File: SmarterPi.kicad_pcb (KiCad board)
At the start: 2 copper layers, 56 x 65 mm, 8 parts, among them J1 Raspberry_Pi_2_3, J2 RJ10

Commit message: Reed
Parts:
- added J3: Screw_Terminal_01x02, TerminalBlock:TerminalBlock_bornier-2_P5.08mm, F.Cu at (92.3, 80.2)
- added J4: Screw_Terminal_01x02, TerminalBlock:TerminalBlock_bornier-2_P5.08mm, F.Cu at (105.8, 80.2)
- added R1: 2k4, Resistor_THT:R_Axial_DIN0207_L6.3mm_D2.5mm_P10.16mm_Horizontal, F.Cu at (89.8, 86.1)
- added REF**: KiCad-Logo2_8mm_SilkScreen, Symbol:KiCad-Logo2_8mm_SilkScreen, B.Cu at (110.5, 130.1)
- moved REF** 2.99 mm to (128.0, 131.1)
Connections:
- J1 pad 15: Net-(J1-Pad15) -> REED
- J1 pad 17: +3V3 -> Net-(J1-Pad17)
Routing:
- net REED: track 0.00 -> 45.2 mm
- net +3V3: track 18.7 -> 63.0 mm
- net +5V: track 0.00 -> 2.54 mm
- added copper zone on B.Cu, net GND
- added copper zone on F.Cu, net GND
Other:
- board text added: "B"
- board text added: "G"
- board text added: "GPIO22 = Reed (pulled down)"
- board text added: "haus-automatisierung.com - v0.1"
- board text removed: "v0.1"

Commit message: 1Wire
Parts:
- added R2: 4,7kΩ, Resistor_THT:R_Axial_DIN0207_L6.3mm_D2.5mm_P10.16mm_Horizontal, F.Cu at (89.5, 86.1)
- J3: value Screw_Terminal_01x02 -> Screw_Terminal_01x04; footprint TerminalBlock:TerminalBlock_bornier-2_P5.08mm -> TerminalBlock_Phoenix:TerminalBlock_Phoenix_MPT-0,5-4-2.54_1x04_P2.54mm_Horizontal
- J4: value Screw_Terminal_01x02 -> Screw_Terminal_01x03; footprint TerminalBlock:TerminalBlock_bornier-2_P5.08mm -> TerminalBlock_Phoenix:TerminalBlock_Phoenix_MPT-0,5-3-2.54_1x03_P2.54mm_Horizontal
- R1: value 2k4 -> 2,4kΩ
- moved R1 23.3 mm to (113.1, 86.1), turned to 180 degrees
- moved J3 19.5 mm to (111.8, 80.5), turned to 180 degrees
- moved J4 8.70 mm to (97.2, 80.5), turned to 180 degrees
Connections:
- J1 pad 7: Net-(J1-Pad7) -> 1Wire
- J4 pad 1: Net-(J4-Pad1) -> +3V3
- J4 pad 2: Net-(J4-Pad2) -> 1Wire
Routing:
- net 1Wire: track 0.00 -> 56.3 mm
- net REED: track 45.2 -> 42.0 mm
- net Net-(J3-Pad4): track 0.00 -> 0.94 mm
- net +3V3: track 63.0 -> 62.5 mm
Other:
- board text added: "+"
- board text added: "1Wire"
- board text added: "D"
- board text added: "GND"
- board text added: "GPIO22 = Reed (pulled down) GPIO4 = 1Wire"
- board text added: "REED"
- board text removed: "GPIO22 = Reed (pulled down)"

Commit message: Readme, License, Preview
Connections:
- J4 pad 1: +3V3 -> +5V
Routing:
- net +5V: track 2.54 -> 42.7 mm
- net +3V3: track 62.5 -> 52.8 mm
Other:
- board text added: "2.4kΩ"
- board text added: "4.7kΩ"
- board text added: "VCC"
- board text removed: "+"

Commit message: Added LEDs
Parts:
- added D1: LED, LED_SMD:LED_0805_2012Metric_Pad1.15x1.40mm_HandSolder, F.Cu at (123.6, 116.7)
- added D2: LED, LED_SMD:LED_0805_2012Metric_Pad1.15x1.40mm_HandSolder, F.Cu at (123.7, 119.2)
- added D3: LED, LED_SMD:LED_0805_2012Metric_Pad1.15x1.40mm_HandSolder, F.Cu at (123.7, 121.7)
- added R3: 330Ω, Resistor_SMD:R_0805_2012Metric_Pad1.20x1.40mm_HandSolder, F.Cu at (128.1, 116.7)
- added R4: 330Ω, Resistor_SMD:R_0805_2012Metric_Pad1.20x1.40mm_HandSolder, F.Cu at (128.1, 119.2)
- added R5: 330Ω, Resistor_SMD:R_0805_2012Metric_Pad1.20x1.40mm_HandSolder, F.Cu at (128.2, 121.7)
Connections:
- J1 pad 29: Net-(J1-Pad29) -> GPIO5
- J1 pad 31: Net-(J1-Pad31) -> GPIO6
- J1 pad 33: Net-(J1-Pad33) -> GPIO13
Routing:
- net GPIO5: track 0.00 -> 3.82 mm
- net GPIO6: track 0.00 -> 3.79 mm
- net GPIO13: track 0.00 -> 3.77 mm
- net Net-(D3-Pad2): track 0.00 -> 2.49 mm
- net Net-(D1-Pad2): track 0.00 -> 2.45 mm
- net Net-(D2-Pad2): track 0.00 -> 2.45 mm
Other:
- board text added: "GPIO22 = Reed (pulled down) GPIO4 = 1Wire GPIO5 = LED GPIO6 = LED GPIO13 = LED"
- board text added: "W"
- board text added: "Y"
- board text removed: "GPIO22 = Reed (pulled down) GPIO4 = 1Wire"

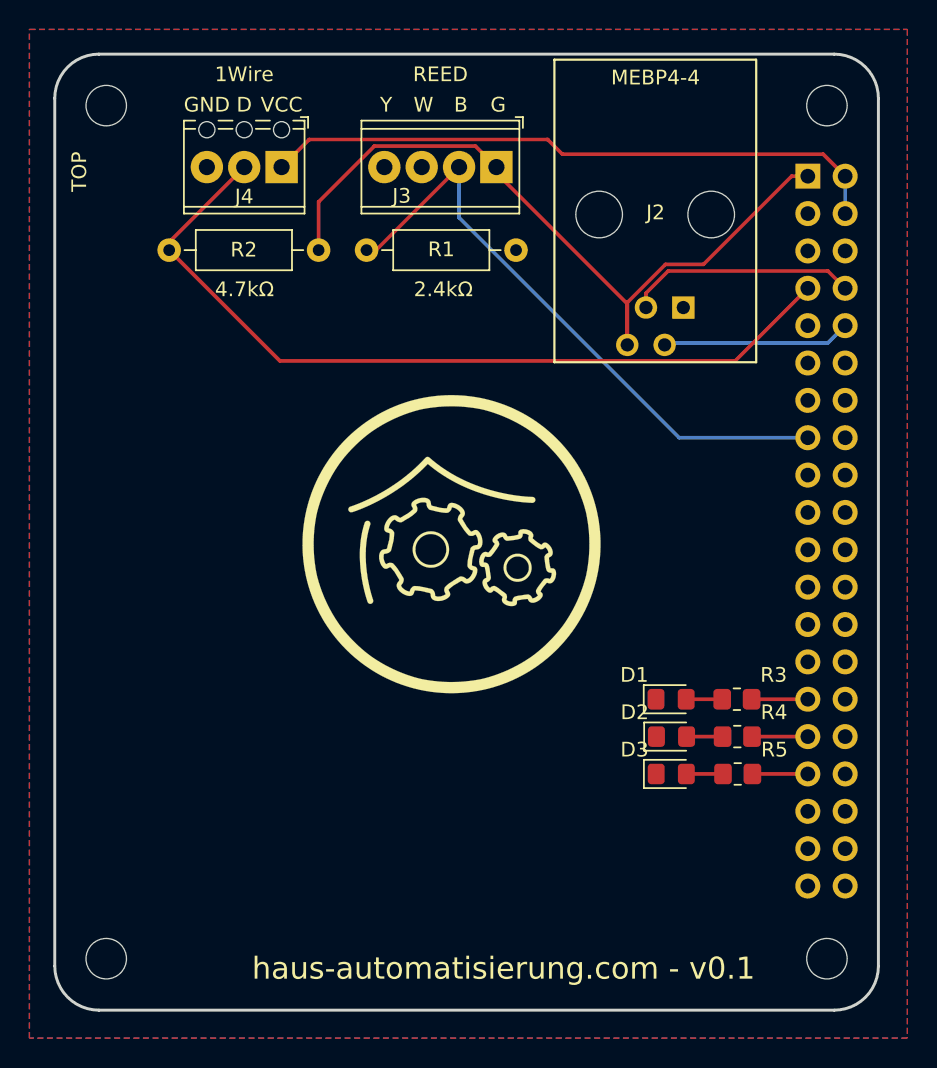
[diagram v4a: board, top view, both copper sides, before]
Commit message: Added 3 push buttons
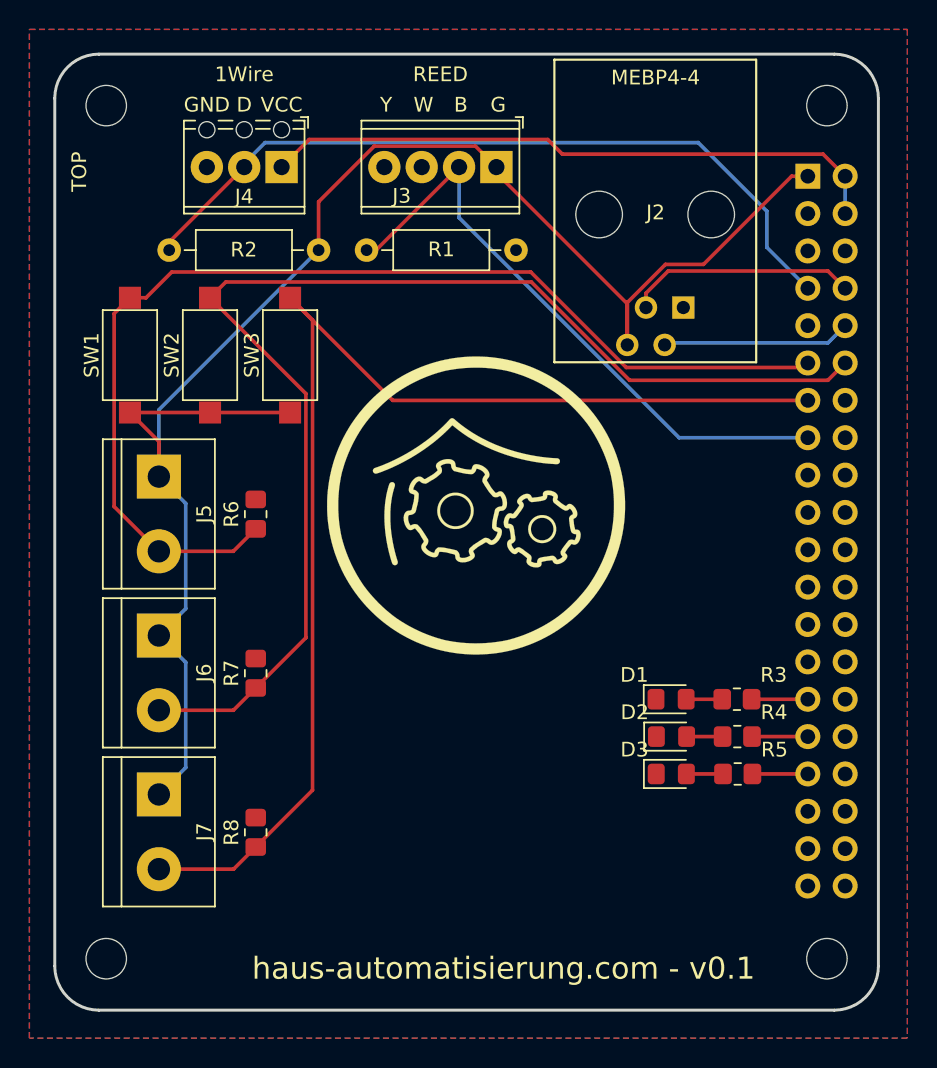
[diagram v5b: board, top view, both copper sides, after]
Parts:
- added J5: Screw_Terminal_01x02, TerminalBlock:TerminalBlock_bornier-2_P5.08mm, F.Cu at (88.8, 101.5)
- added J6: Screw_Terminal_01x02, TerminalBlock:TerminalBlock_bornier-2_P5.08mm, F.Cu at (88.8, 112.3)
- added J7: Screw_Terminal_01x02, TerminalBlock:TerminalBlock_bornier-2_P5.08mm, F.Cu at (88.8, 123.1)
- added R6: 10kΩ, Resistor_SMD:R_0805_2012Metric_Pad1.20x1.40mm_HandSolder, F.Cu at (95.4, 104.1)
- added R7: 10kΩ, Resistor_SMD:R_0805_2012Metric_Pad1.20x1.40mm_HandSolder, F.Cu at (95.4, 114.9)
- added R8: 10kΩ, Resistor_SMD:R_0805_2012Metric_Pad1.20x1.40mm_HandSolder, F.Cu at (95.4, 125.7)
- added SW1: SW_Push, Button_Switch_SMD:SW_SPST_CK_RS282G05A3, F.Cu at (86.8, 93.3)
- added SW2: SW_Push, Button_Switch_SMD:SW_SPST_CK_RS282G05A3, F.Cu at (92.3, 93.3)
- added SW3: SW_Push, Button_Switch_SMD:SW_SPST_CK_RS282G05A3, F.Cu at (97.7, 93.3)
- moved G*** 3.12 mm to (110.4, 103.5)
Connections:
- J1 pad 11: Net-(J1-Pad11) -> GPIO17
- J1 pad 12: Net-(J1-Pad12) -> GPIO18
- J1 pad 13: Net-(J1-Pad13) -> GPIO27
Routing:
- net GPIO27: track 0.00 -> 84.9 mm
- net GPIO18: track 0.00 -> 84.7 mm
- net GPIO17: track 0.00 -> 75.8 mm
- net +3V3: track 52.8 -> 113.4 mm
- net 1Wire: track 56.3 -> 52.5 mm
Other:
- board text added: "GPIO22 = Reed (pulled down) GPIO4 = 1Wire GPIO5 = LED GPIO6 = LED GPIO13 = LED GPIO17 = Button GPIO18 = Button GPIO27 = Button"
- board text removed: "2.4kΩ"
- board text removed: "4.7kΩ"
- board text removed: "GPIO22 = Reed (pulled down) GPIO4 = 1Wire GPIO5 = LED GPIO6 = LED GPIO13 = LED"

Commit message: Minor fixes
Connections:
- J1 pad 6: GND -> Net-(J1-Pad6)
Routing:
- net REED: track 42.0 -> 42.2 mm, vias 0 -> 1
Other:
- board text added: "Smarter Pi v0.1"
- board text removed: "haus-automatisierung.com - v0.1"

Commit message: 0.1
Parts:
- R1: value 2,4kΩ -> 2,2kΩ

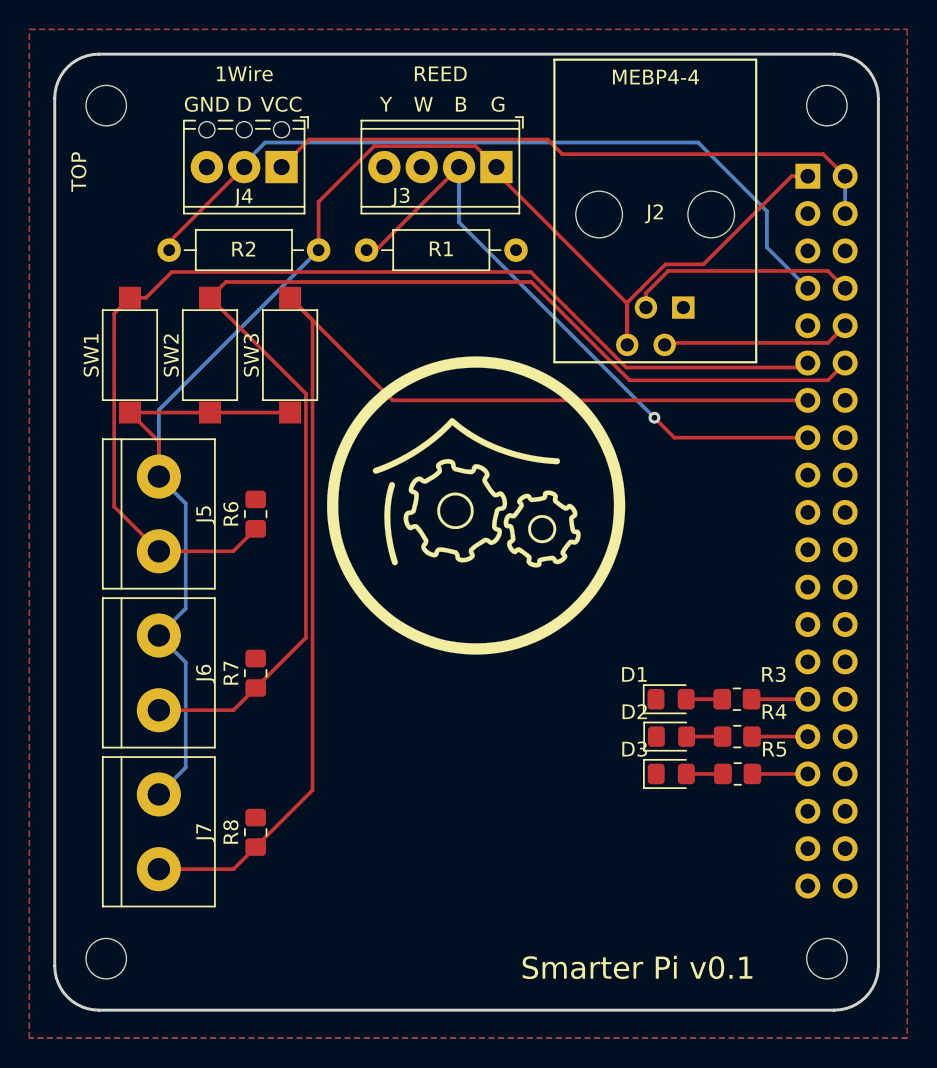
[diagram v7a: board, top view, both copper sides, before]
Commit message: Smaller terminal block for buttons
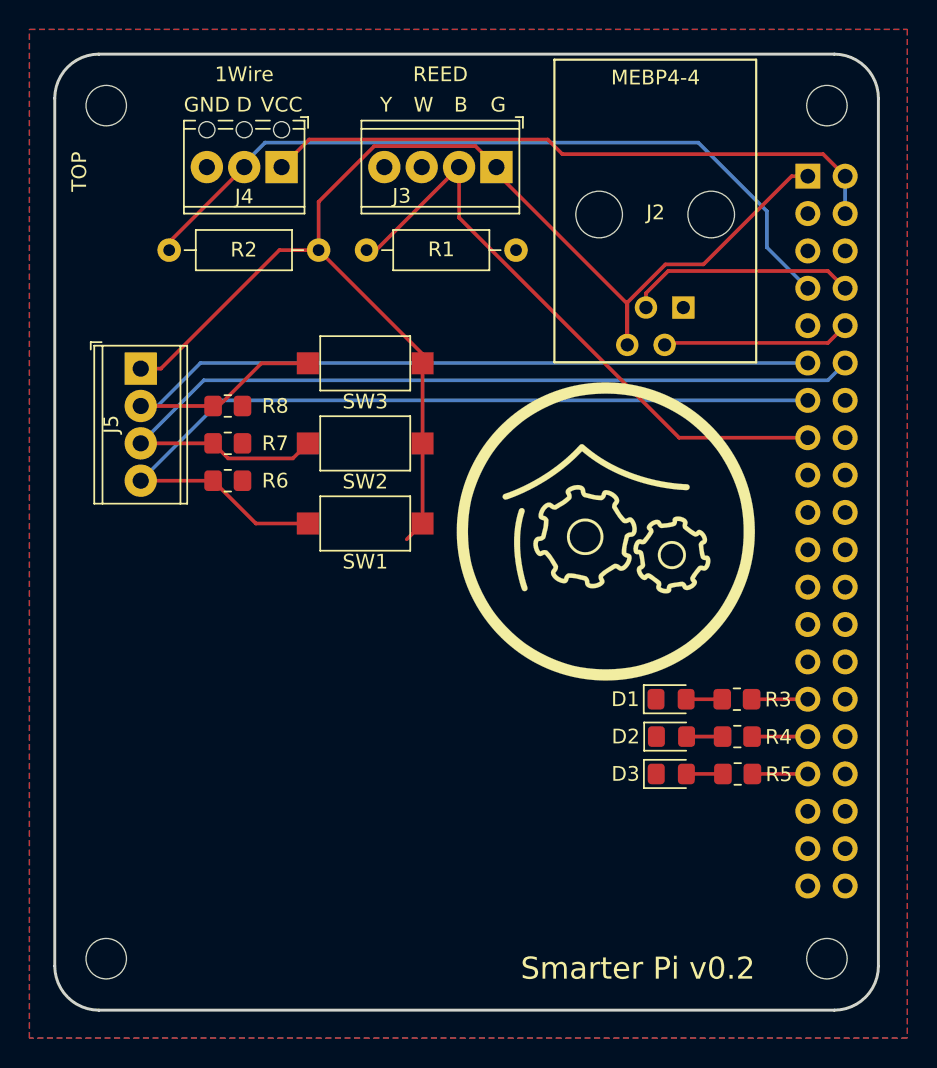
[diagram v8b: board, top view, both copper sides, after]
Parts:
- removed J6, J7: Screw_Terminal_01x02, TerminalBlock:TerminalBlock_bornier-2_P5.08mm
- J5: value Screw_Terminal_01x02 -> Screw_Terminal_01x04; footprint TerminalBlock:TerminalBlock_bornier-2_P5.08mm -> TerminalBlock_Phoenix:TerminalBlock_Phoenix_MPT-0,5-4-2.54_1x04_P2.54mm_Horizontal
- moved R8 29.0 mm to (93.5, 96.7), turned to 0 degrees
- moved SW1 19.7 mm to (102.8, 104.7), turned to 180 degrees
- moved R7 15.7 mm to (93.5, 99.3), turned to 0 degrees
- moved SW2 12.1 mm to (102.8, 99.3), turned to 180 degrees
- moved G*** 8.99 mm to (119.2, 105.3)
- moved J5 7.44 mm to (87.6, 94.2)
- moved SW3 5.14 mm to (102.8, 93.8), turned to 180 degrees
- moved R6 2.96 mm to (93.5, 101.8), turned to 0 degrees
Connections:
- R6 pad 1: GPIO17 -> GPIO27
- R8 pad 1: GPIO27 -> GPIO17
- SW1 pad 2: GPIO17 -> GPIO27
- SW3 pad 2: GPIO27 -> GPIO17
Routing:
- net GPIO27: track 84.9 -> 60.2 mm
- net GPIO18: track 84.7 -> 62.4 mm
- net +3V3: track 113.4 -> 91.3 mm
- net GPIO17: track 75.8 -> 59.6 mm
- net REED: track 42.2 -> 42.0 mm, vias 1 -> 0
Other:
- board text added: "Smarter Pi v0.2"
- board text removed: "Smarter Pi v0.1"
